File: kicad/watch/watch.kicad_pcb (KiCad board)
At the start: 2 copper layers, 35.6 x 25.4 mm, 36 parts, among them J1 USB_C_Receptacle_USB2.0, J2 Conn_01x04_Female, J3 Conn_01x04_Female, J4 Memory LCD, J5 LCD Frontlight, Q1 Q_NMOS_GDS, SW1 SW_Push, SW2 SW_Push, U1 E73-2G4M08S1C-52840, U2 MCP73831-2-OT, U3 DS1302S+, U4 TPS63001, Y1 Crystal, Y2 32.768 kHz

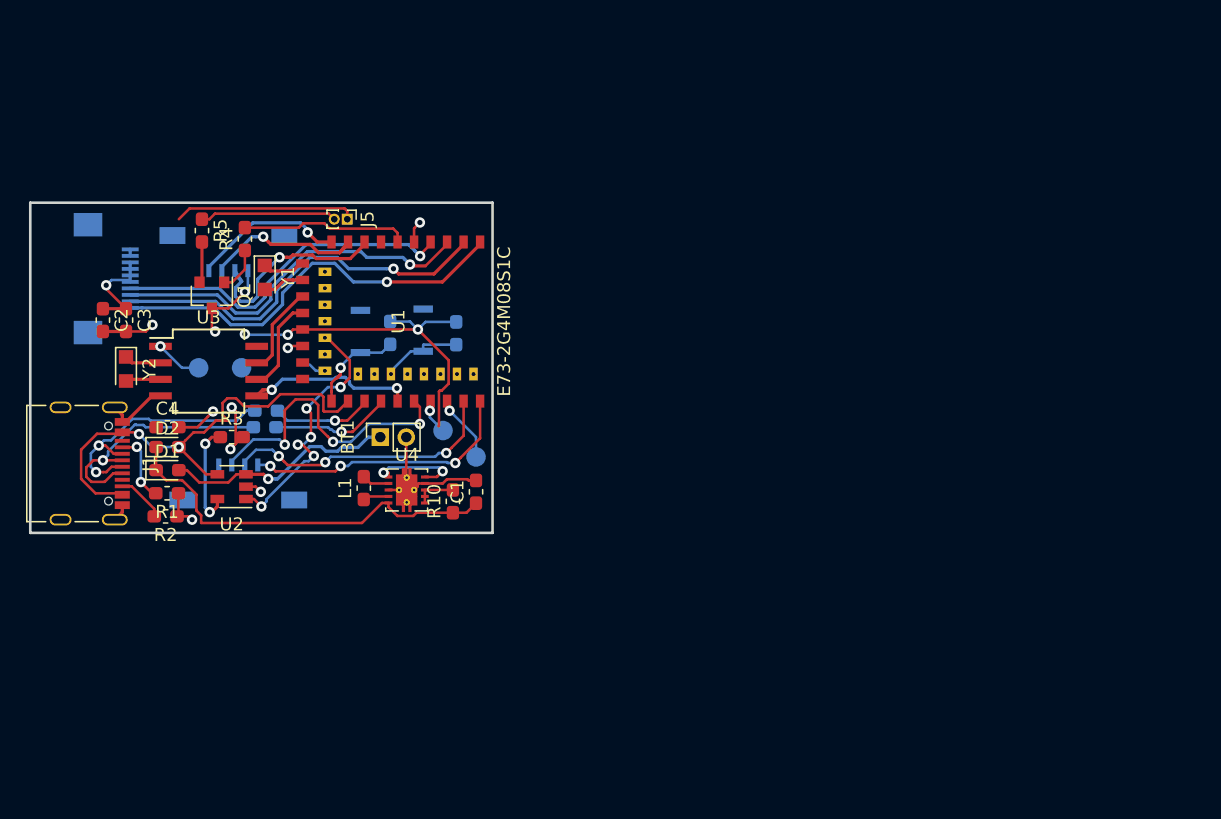
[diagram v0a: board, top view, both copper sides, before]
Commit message: Second rev of schematic. Not yet routed.
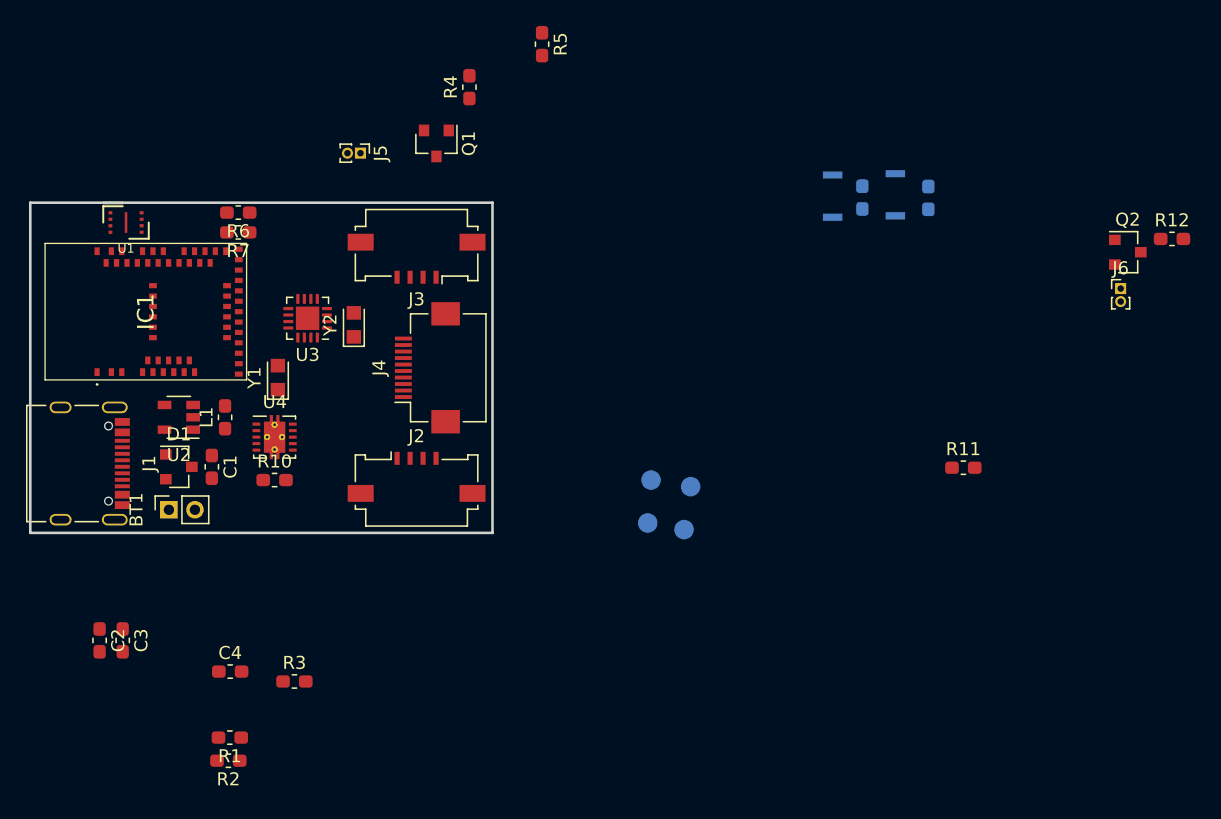
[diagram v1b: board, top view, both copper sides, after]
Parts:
- removed D2: D_Schottky, Diode_SMD:D_0603_1608Metric_Pad1.05x0.95mm_HandSolder
- added IC1: 113990582, 113990582:113990582, F.Cu at (8.89, 8.38)
- added J6: Buzzer, Connector_PinHeader_1.00mm:PinHeader_1x02_P1.00mm_Vertical, F.Cu at (83.9, 6.61)
- added Q2: Q_NMOS_GDS, Package_TO_SOT_SMD:SOT-23, F.Cu at (84.4, 3.81)
- added R11: R, Resistor_SMD:R_0603_1608Metric_Pad1.05x0.95mm_HandSolder, F.Cu at (71.8, 20.4)
- added R12: R, Resistor_SMD:R_0603_1608Metric_Pad1.05x0.95mm_HandSolder, F.Cu at (87.8, 2.79)
- D1: value D_Schottky -> D_Schottky_x2_KCom_AAK; footprint Diode_SMD:D_0603_1608Metric_Pad1.05x0.95mm_HandSolder -> Package_TO_SOT_SMD:SOT-23
- J2, J3, J4, R6, R7: moved to F.Cu
- U1: value E73-2G4M08S1C-52840 -> W25X20CLUXIG; footprint nrfmicro:E73-2G4M08S1C-52840 -> libs:8-USON
- U3: value DS1302S+ -> M41T62Q; footprint Package_SO:SO-8_5.3x6.2mm_P1.27mm -> Package_DFN_QFN:VQFN-16-1EP_3x3mm_P0.5mm_EP1.8x1.8mm
- moved TP1 39.4 mm to (50.3, 25.1)
- moved SW1 37.8 mm to (61.7, -0.51)
- moved SW2 37.8 mm to (66.5, -0.61)
- moved R8 37.8 mm to (64.0, -0.40)
- moved R9 37.8 mm to (69.1, -0.37)
- moved TP2 32.7 mm to (47.8, 21.3)
- moved R5 29.8 mm to (39.4, -12.2)
- moved J4 25.6 mm to (30.6, 12.7)
- moved C2 24.6 mm to (5.33, 33.7)
- moved C3 24.6 mm to (7.11, 33.7)
- moved J2 21.8 mm to (29.7, 20.6)
- moved J3 21.3 mm to (29.7, 4.83)
- moved Q1 20.9 mm to (31.2, -4.56)
- moved R4 20.9 mm to (33.8, -8.89)
- moved C1 20.4 mm to (14.0, 20.3), turned to 270 degrees
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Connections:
- D1 pad 1: VIN -> VBUS
- J4 pad 4: EXTCOMIN -> SQW
- J4 pad 8: +3V3 -> EXTMODE
- Q1 pad 1: Net-(Q1-Pad1) -> FRONTLIGHT
- R4 pad 1: Net-(Q1-Pad1) -> GND
- R6 pad 2: Net-(R6-Pad2) -> Net-(IC1-Pad35)
- R7 pad 2: Net-(R7-Pad2) -> Net-(IC1-Pad34)
- U1 pad 1: LCD_CLK -> FLASH_CS
- U1 pad 2: LCD_MOSI -> FLASH_DO
- U1 pad 3: LCD_CS -> +3V3
- U1 pad 4: EXTCOMIN -> GND
- U1 pad 5: GND -> FLASH_DI
- U1 pad 6: FRONTLIGHT -> FLASH_CLK
- U1 pad 7: (no net) -> +3V3
- U1 pad 8: BTN3 -> +3V3
- U2 pad 1: CHRG_STAT -> (no net)
- U3 pad 1: +3V3 -> Net-(U3-Pad1)
- U3 pad 3: Net-(U3-Pad3) -> (no net)
- U3 pad 4: GND -> SQW
- U3 pad 5: RTC_CS -> GND
- U3 pad 6: RTC_IO -> (no net)
- U3 pad 7: RTC_CLK -> (no net)
- Y1 pad 1: Net-(U1-Pad11) -> Net-(IC1-Pad17)
- Y1 pad 2: Net-(U1-Pad13) -> Net-(IC1-Pad18)
- Y2 pad 1: Net-(U3-Pad2) -> Net-(U3-Pad1)
- Y2 pad 2: Net-(U3-Pad3) -> Net-(U3-Pad2)
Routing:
- net +3V3: track 60.7 -> 0.00 mm, vias 7 -> 0
- net GND: track 44.7 -> 0.00 mm, vias 10 -> 0
- net VBUS: track 36.4 -> 0.00 mm, vias 2 -> 0
- net LCD_CLK: track 31.9 -> 0.00 mm, vias 1 -> 0
- net VIN: track 30.8 -> 0.00 mm
- net LCD_MOSI: track 30.3 -> 0.00 mm, vias 1 -> 0
- net LCD_CS: track 28.7 -> 0.00 mm, vias 1 -> 0
- net EXTCOMIN: track 27.4 -> 0.00 mm, vias 1 -> 0
- net BTN6: track 23.5 -> 0.00 mm, vias 3 -> 0
- net BTN5: track 21.6 -> 0.00 mm, vias 3 -> 0
- net BTN4: track 21.3 -> 0.00 mm, vias 3 -> 0
- net CHRG_STAT: track 20.6 -> 0.00 mm, vias 6 -> 0
- net USB_DN: track 20.0 -> 0.00 mm, vias 2 -> 0
- net USB_DP: track 19.9 -> 0.00 mm, vias 1 -> 0
- net +BATT: track 17.9 -> 0.00 mm, vias 1 -> 0
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
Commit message: routed board rev2
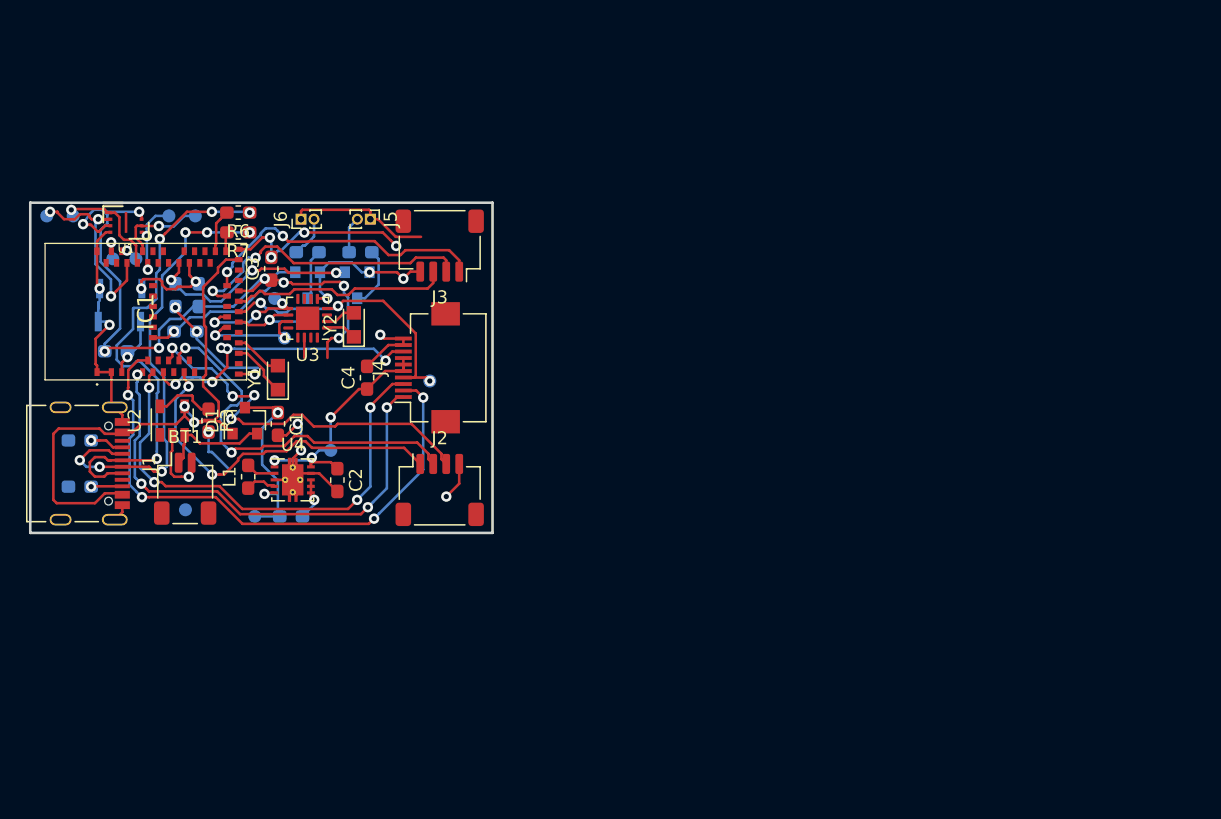
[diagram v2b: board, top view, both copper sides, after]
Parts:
- added TP10: TestPoint, TestPoint:TestPoint_Pad_D1.0mm, B.Cu at (12.7, 1.02)
- added TP11: TestPoint, TestPoint:TestPoint_Pad_D1.0mm, B.Cu at (3.30, 1.02)
- added TP12: TestPoint, TestPoint:TestPoint_Pad_D1.0mm, B.Cu at (1.27, 1.02)
- added TP13: TestPoint, TestPoint:TestPoint_Pad_D1.0mm, B.Cu at (17.3, 24.1)
- added TP5: TestPoint, TestPoint:TestPoint_Pad_D1.0mm, B.Cu at (21.3, 9.14)
- added TP6: TestPoint, TestPoint:TestPoint_Pad_D1.0mm, B.Cu at (18.8, 7.37)
- added TP7: TestPoint, TestPoint:TestPoint_Pad_D1.0mm, B.Cu at (30.7, 13.7)
- added TP8: TestPoint, TestPoint:TestPoint_Pad_D1.0mm, B.Cu at (19.6, 10.4)
- added TP9: TestPoint, TestPoint:TestPoint_Pad_D1.0mm, B.Cu at (10.7, 1.02)
- BT1: footprint Connector_PinSocket_2.00mm:PinSocket_1x02_P2.00mm_Vertical -> Connector_JST:JST_SH_SM02B-SRSS-TB_1x02-1MP_P1.00mm_Horizontal
- J2, J3: footprint Connector_FFC-FPC:Molex_200528-0040_1x04-1MP_P1.00mm_Horizontal -> Connector_JST:JST_SH_SM04B-SRSS-TB_1x04-1MP_P1.00mm_Horizontal
- Q1, Q2: value Q_NMOS_GDS -> DMN6140L; moved to B.Cu
- R1, R10, R11, R12, R2, R4, R5: moved to B.Cu
- TP1, TP2, TP3, TP4: footprint TestPoint:TestPoint_Pad_D1.5mm -> TestPoint:TestPoint_Pad_D1.0mm
- moved R12 66.5 mm to (21.3, 3.81)
- moved R9 63.6 mm to (6.60, 11.4), turned to 0 degrees
- moved J6 63.3 mm to (20.8, 1.27), turned to 90 degrees
- moved Q2 63.1 mm to (21.3, 6.35), turned to 270 degrees
- moved R11 60.8 mm to (11.9, 9.91), turned to 180 degrees
- moved SW2 60.5 mm to (6.86, 9.14), turned to 180 degrees
- moved SW1 55.2 mm to (6.96, 6.60), turned to 180 degrees
- moved R8 51.6 mm to (13.0, 7.11), turned to 90 degrees
- moved TP4 46.1 mm to (8.13, 4.32)
- moved TP3 45.9 mm to (6.35, 4.32)
- moved TP2 35.9 mm to (11.9, 23.6)
- moved C3 30.8 mm to (18.5, 5.08), turned to 90 degrees
- moved TP1 27.9 mm to (23.1, 19.1)
- moved R4 27.7 mm to (11.2, 7.11)
- moved R1 25.6 mm to (3.81, 18.3), turned to 0 degrees
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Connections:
- IC1 pad 10: BTN3 -> (no net)
- IC1 pad 26: (no net) -> BTN6
- IC1 pad 27: (no net) -> BTN5
- IC1 pad 29: (no net) -> BTN4
- IC1 pad 44: BTN4 -> (no net)
- IC1 pad 45: BTN5 -> (no net)
- IC1 pad 46: BTN6 -> (no net)
- IC1 pad 47: FLASH_CS -> FLASH_DI
- IC1 pad 49: FLASH_DI -> FLASH_CS
- IC1 pad 9: (no net) -> BTN3
- Q1 pad 2: Net-(Q1-Pad2) -> GND
- Q1 pad 3: GND -> Net-(Q1-Pad3)
- Q2 pad 2: Net-(Q2-Pad2) -> GND
- Q2 pad 3: GND -> Net-(Q2-Pad3)
- R12 pad 2: Net-(Q2-Pad2) -> Net-(Q2-Pad3)
- R5 pad 2: Net-(Q1-Pad2) -> Net-(Q1-Pad3)
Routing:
- net GND: track 0.00 -> 85.9 mm, vias 0 -> 18
- net +3V3: track 0.00 -> 83.8 mm, vias 0 -> 11
- net VBUS: track 0.00 -> 44.9 mm, vias 0 -> 2
- net LCD_MOSI: track 0.00 -> 43.8 mm, vias 0 -> 4
- net USB_DP: track 0.00 -> 38.4 mm, vias 0 -> 4
- net LCD_CLK: track 0.00 -> 37.9 mm, vias 0 -> 4
- net LCD_CS: track 0.00 -> 37.2 mm, vias 0 -> 4
- net USB_DN: track 0.00 -> 35.6 mm, vias 0 -> 6
- net BTN3: track 0.00 -> 30.8 mm, vias 0 -> 4
- net BTN2: track 0.00 -> 30.0 mm, vias 0 -> 2
- net BTN1: track 0.00 -> 27.5 mm, vias 0 -> 2
- net SQW: track 0.00 -> 23.0 mm, vias 0 -> 3
- net BTN4: track 0.00 -> 22.7 mm, vias 0 -> 2
- net EXTMODE: track 0.00 -> 22.7 mm, vias 0 -> 5
- net BTN5: track 0.00 -> 22.7 mm, vias 0 -> 2
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
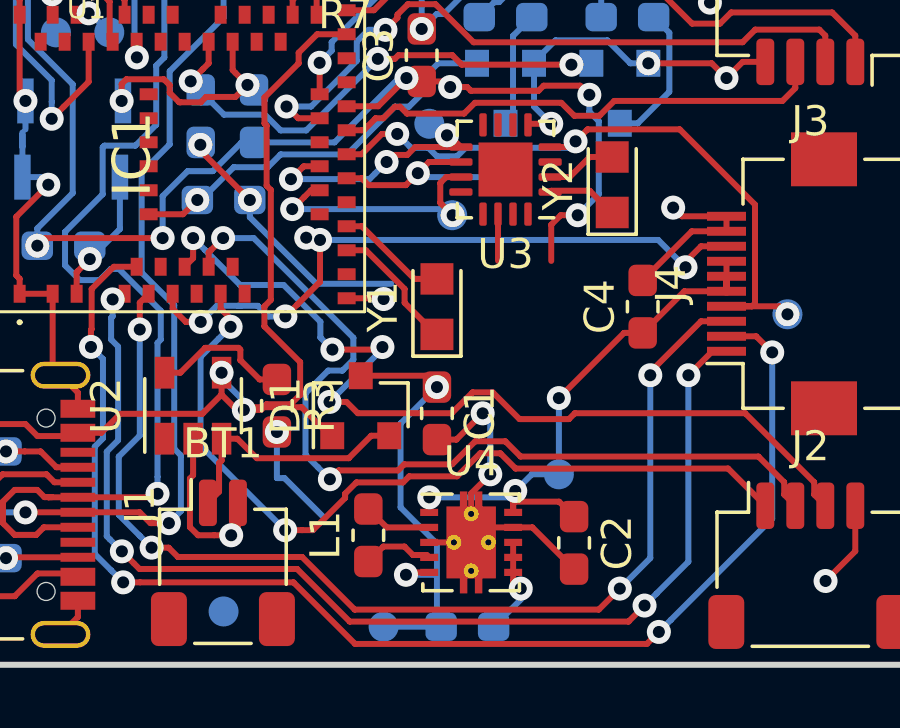
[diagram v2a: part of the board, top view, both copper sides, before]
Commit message: added voltage divider for battery reading
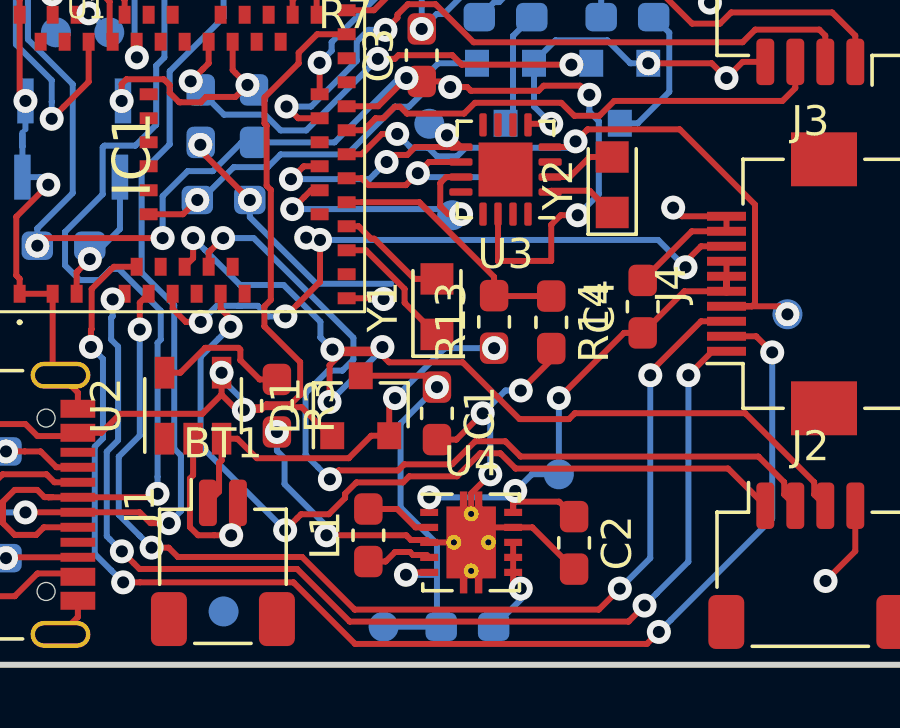
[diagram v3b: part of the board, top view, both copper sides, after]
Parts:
- added R13: 2M, Resistor_SMD:R_0603_1608Metric_Pad1.05x0.95mm_HandSolder, F.Cu at (21.0, 14.0)
- added R14: 4M, Resistor_SMD:R_0603_1608Metric_Pad1.05x0.95mm_HandSolder, F.Cu at (22.9, 14.0)
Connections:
- IC1 pad 20: (no net) -> BATREAD
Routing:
- net BATREAD: track 0.00 -> 8.48 mm
- net GND: track 85.9 -> 93.3 mm, vias 18 -> 20
- net +BATT: track 8.49 -> 13.8 mm, vias 0 -> 2
- net +3V3: track 83.8 -> 85.6 mm
- net BTN3: track 30.8 -> 32.3 mm
- net RTC_IRQ: track 8.64 -> 9.53 mm

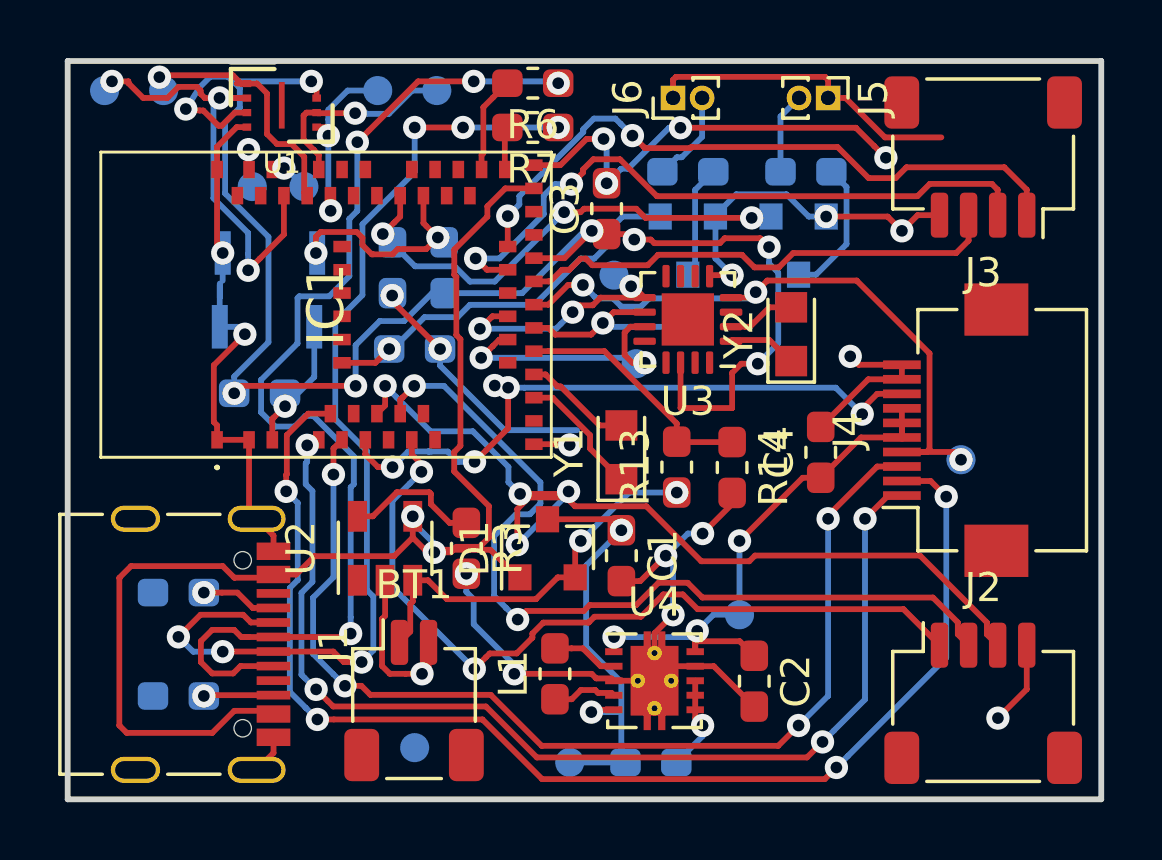
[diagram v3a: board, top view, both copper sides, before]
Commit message: Add qwiic jumpers for accessory ports
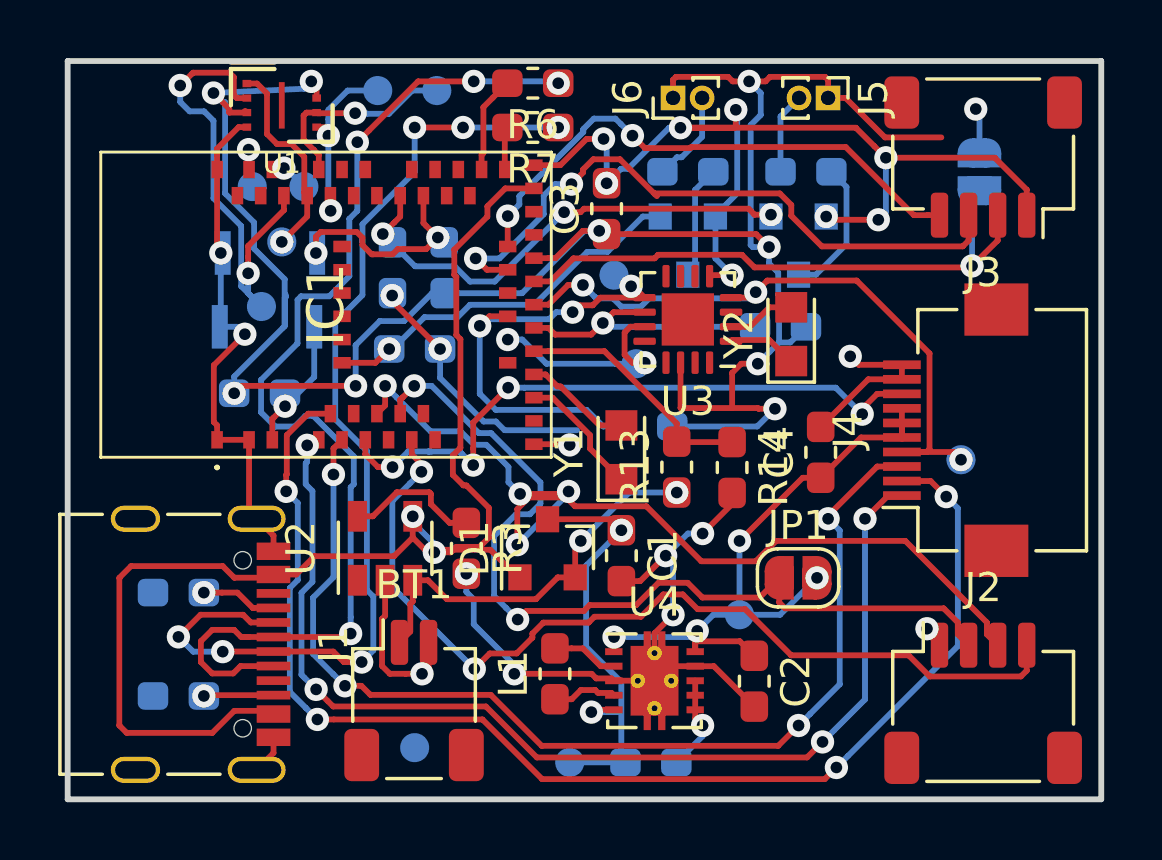
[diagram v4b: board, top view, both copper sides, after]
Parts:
- added JP1: Jumper_NO_Small, Jumper:SolderJumper-2_P1.3mm_Open_RoundedPad1.0x1.5mm, F.Cu at (25.1, 17.8)
- added JP2: Jumper_NO_Small, Jumper:SolderJumper-2_P1.3mm_Open_RoundedPad1.0x1.5mm, B.Cu at (31.4, 3.81)
- added R15: 4k7, Resistor_SMD:R_0603_1608Metric_Pad1.05x0.95mm_HandSolder, B.Cu at (19.9, 12.6)
- added R16: 4k7, Resistor_SMD:R_0603_1608Metric_Pad1.05x0.95mm_HandSolder, B.Cu at (24.5, 9.14)
- moved TP12 9.18 mm to (6.67, 8.45)
- moved TP11 6.61 mm to (7.37, 6.22)
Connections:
- J2 pad 1: BTN1 -> GND
- J2 pad 4: GND -> BTN1
- J3 pad 1: BTN4 -> GND
- J3 pad 2: BTN5 -> BTN6
- J3 pad 3: BTN6 -> BTN5
- J3 pad 4: GND -> BTN4
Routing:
- net +3V3: track 85.6 -> 102.3 mm, vias 11 -> 14
- net SDA: track 8.63 -> 16.2 mm
- net GND: track 93.3 -> 99.6 mm, vias 20 -> 21
- net BTN1: track 27.5 -> 31.9 mm
- net BTN4: track 22.7 -> 18.9 mm
- net BTN6: track 17.0 -> 20.5 mm, vias 0 -> 1
- net SCL: track 7.20 -> 9.52 mm
- net RTC_IRQ: track 9.53 -> 7.66 mm
- net FLASH_CS: track 8.52 -> 7.17 mm
- net BTN2: track 30.0 -> 31.1 mm
- net FLASH_DO: track 16.2 -> 16.8 mm, vias 3 -> 2
- net EXTMODE: track 22.7 -> 22.4 mm, vias 5 -> 4
